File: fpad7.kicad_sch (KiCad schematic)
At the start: 64 parts, among them J2 Conn_01x12, SW1 SW_Push, SW10 SW_Push, SW11 SW_Push, SW12 SW_Push, SW13 SW_Push, SW14 SW_Push, SW15 SW_Push, SW16 SW_Push, SW17 SW_Push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

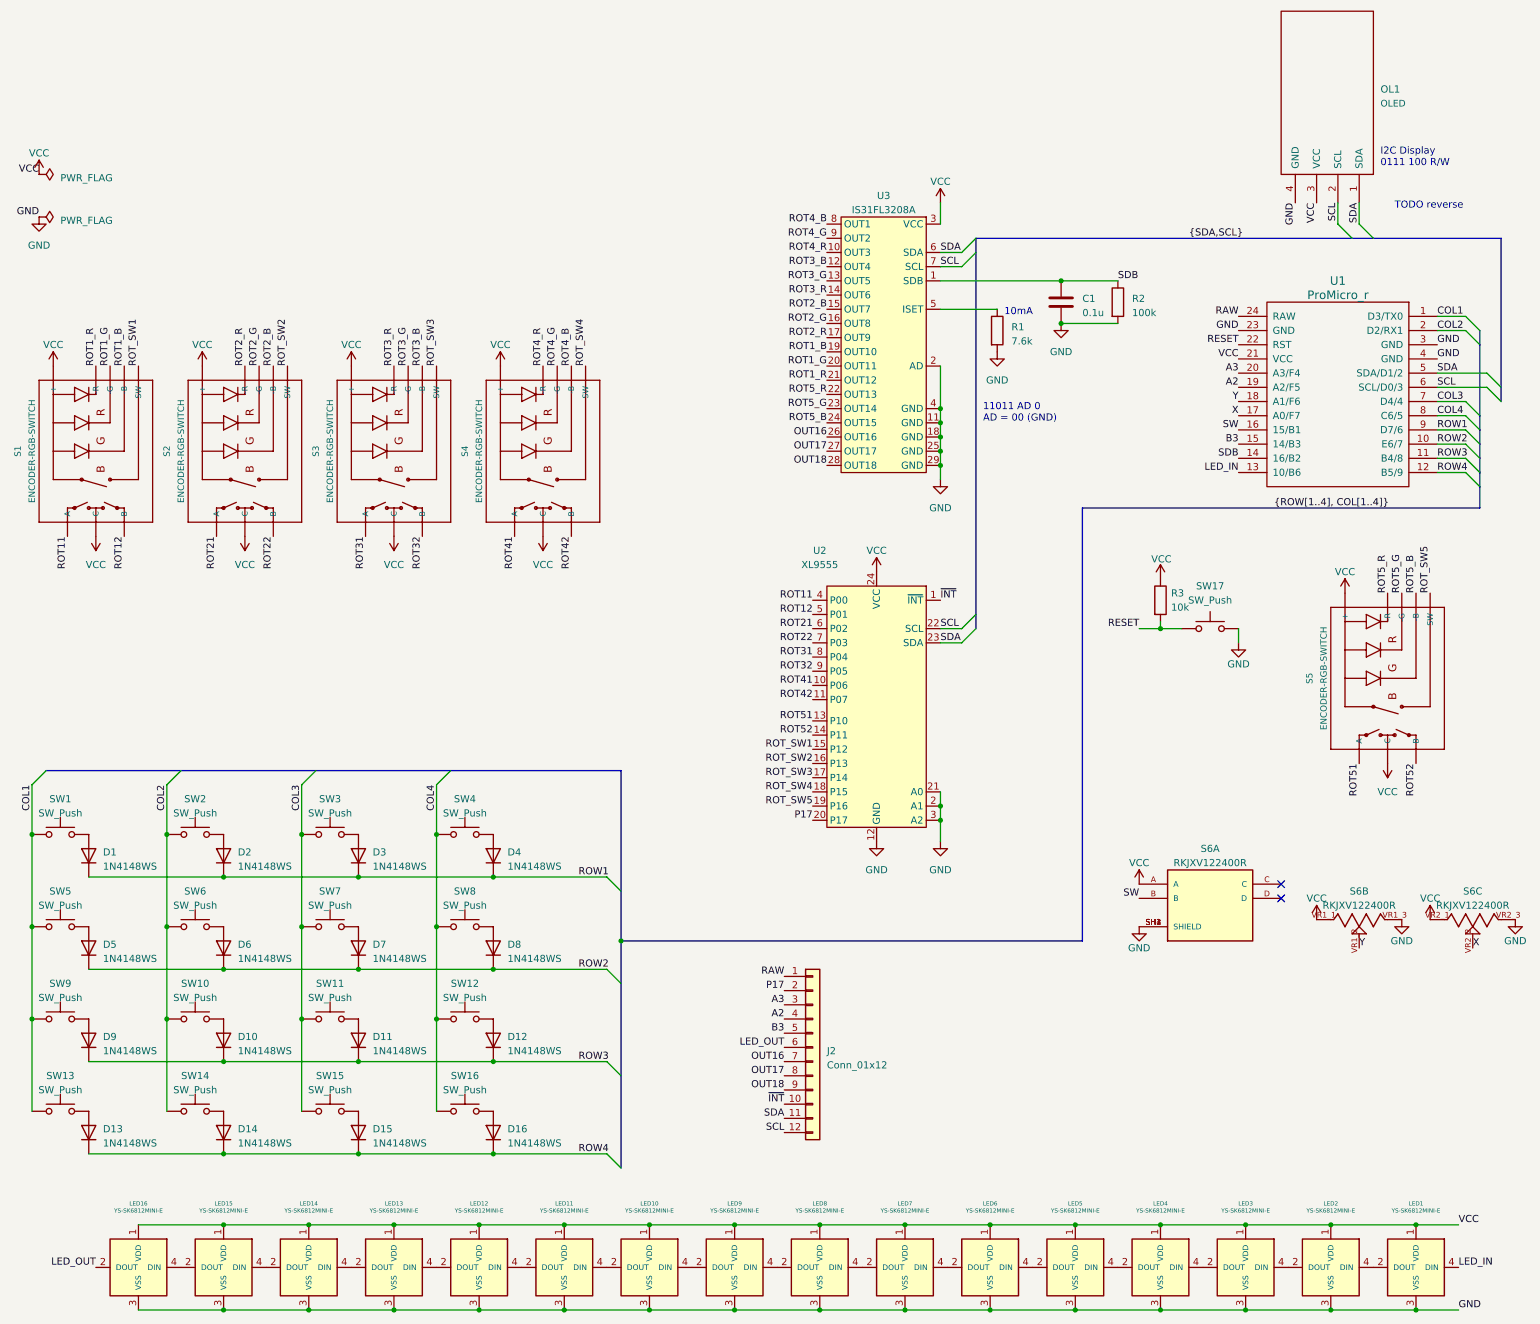
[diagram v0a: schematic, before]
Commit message: update: errata for rev1
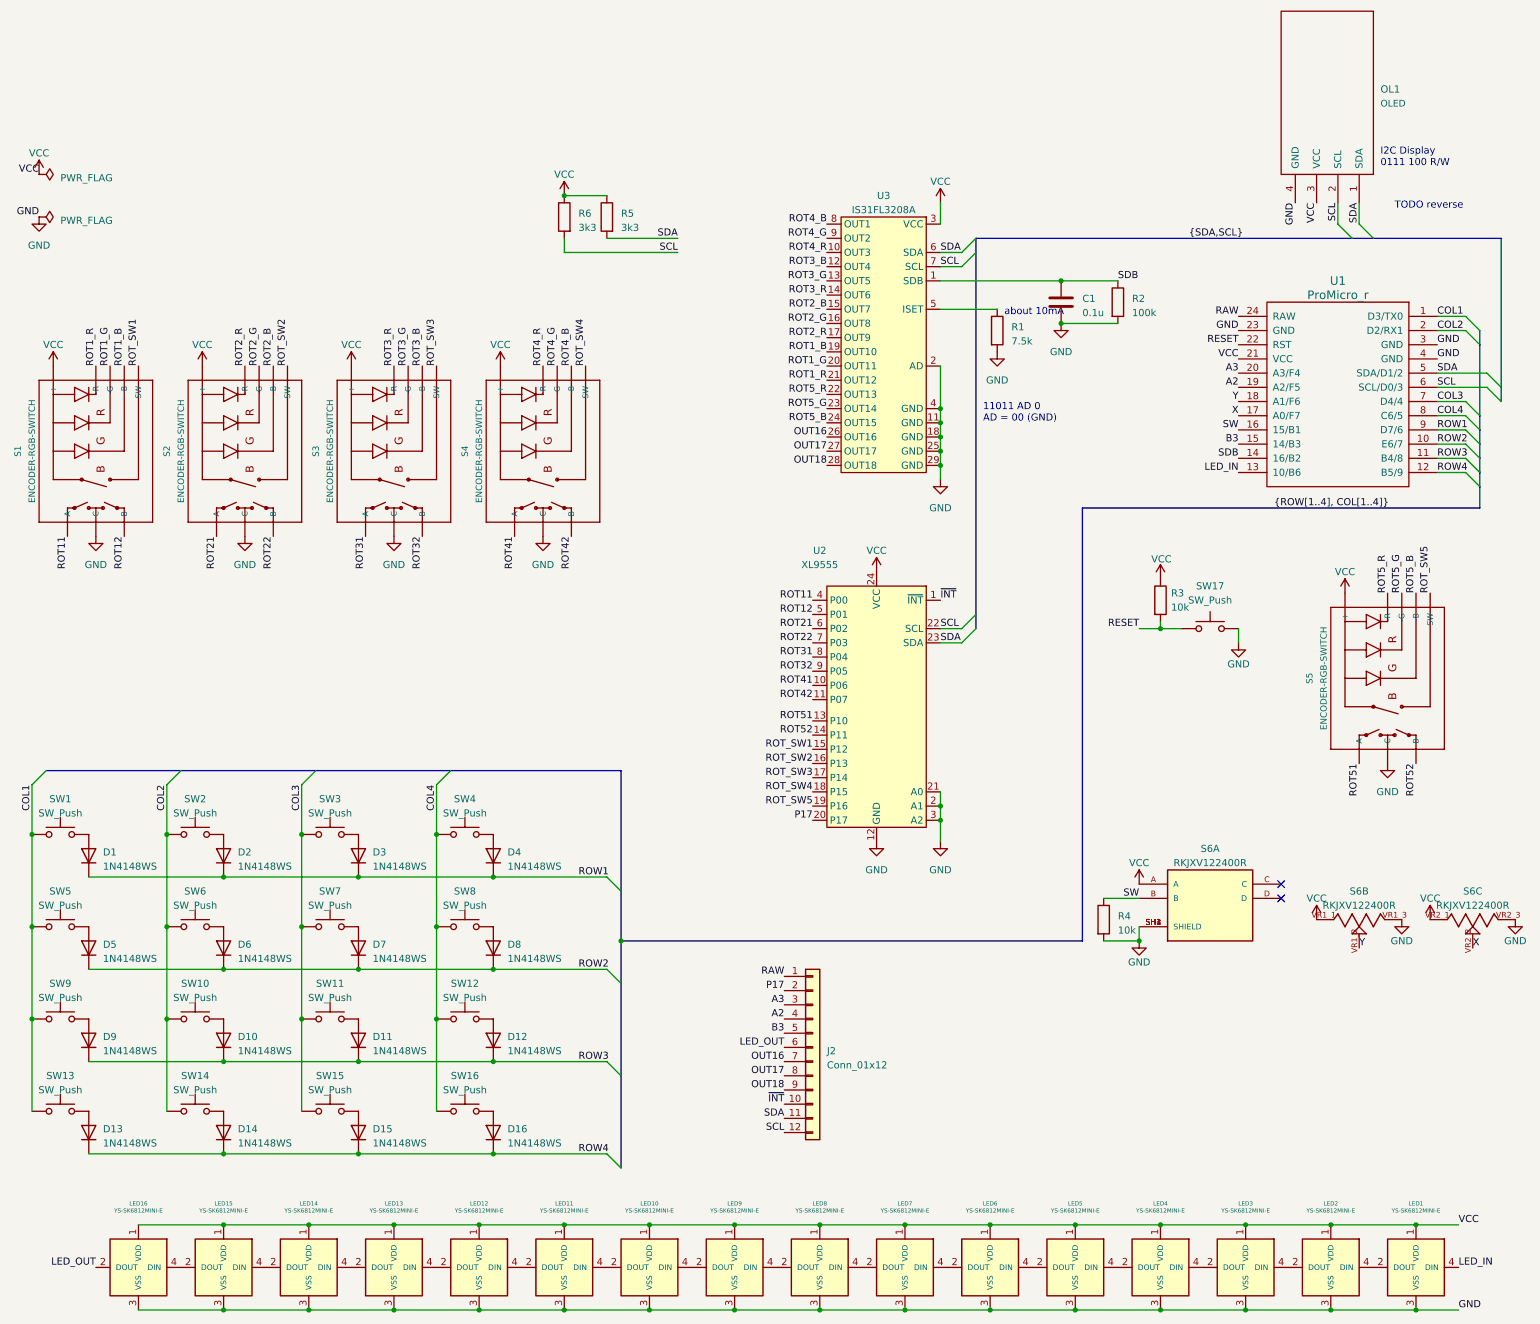
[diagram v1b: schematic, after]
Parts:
- added R4: 10k, Resistor_SMD:R_0402_1005Metric, symbol Device:R
- added R5, R6: 3k3, Resistor_SMD:R_0402_1005Metric, symbol Device:R
- R1: value 7.6k -> 7.5k; LCSC C4109 -> C25918
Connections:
- net GND: now also S1.C, S2.C, S3.C, S4.C, S5.C, R4.2
- net SCL: now also R6.2
- net SDA: now also R5.2
- net SW: now also R4.1
- net VCC: now also R5.1, R6.1; no longer S1.C, S2.C, S3.C, S4.C, S5.C
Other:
- note added: "about 10mA"
- note removed: "10mA"

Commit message: fix: rot sw should be pull down
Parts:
- added R10, R11, R7, R8, R9: 10k, Resistor_SMD:R_0402_1005Metric, symbol Device:R
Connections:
- net GND: now also R10.2, R11.2, R7.2, R8.2, R9.2
- net ROT_SW1: now also R7.1
- net ROT_SW2: now also R8.1
- net ROT_SW3: now also R9.1
- net ROT_SW4: now also R10.1
- net ROT_SW5: now also R11.1
